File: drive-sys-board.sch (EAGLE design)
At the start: 27 parts

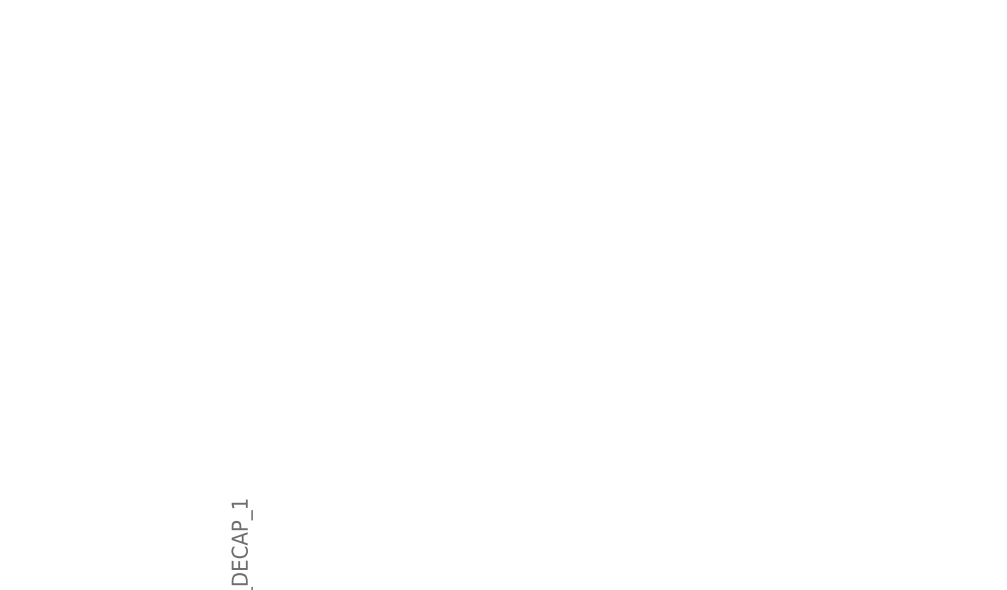
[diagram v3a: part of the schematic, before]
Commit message: okay nvm not finalized... almost used a IEA232 xcvr... need to use the added rs232 xcvr
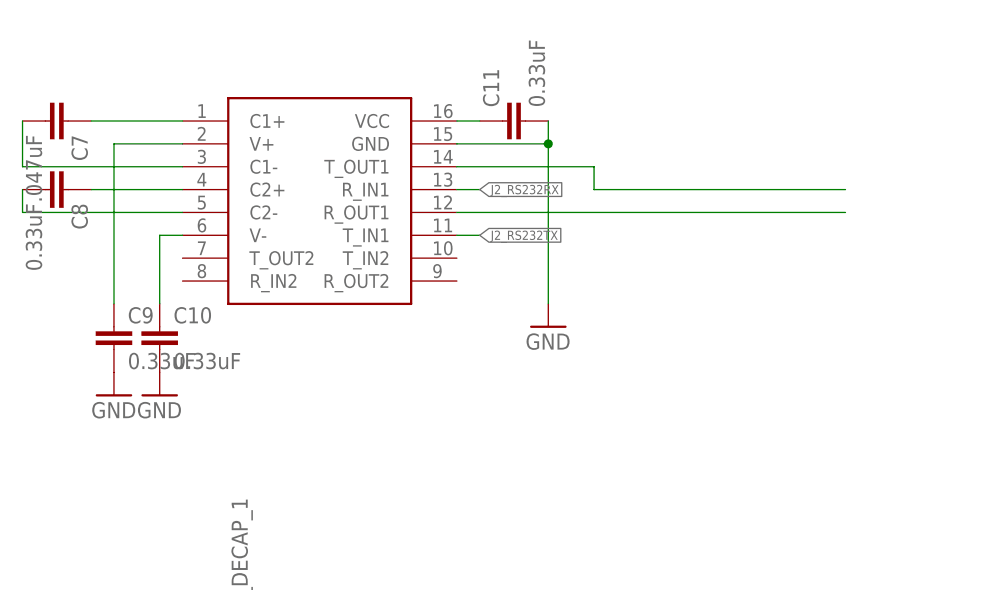
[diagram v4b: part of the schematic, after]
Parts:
- added C10, C11, C8, C9: 0.33uF, SparkFun-Capacitors:CAP1206
- added C7: .047uF, SparkFun-Capacitors:CAP1206
- added MAX232: MAX3232, MRDT-LIB2014:MAX3232
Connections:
- new net J2_RS232RX: MAX232.R_IN1
- new net J2_RS232TX: MAX232.T_IN1
- new net N$15: C7.2, MAX232.C1-
- new net N$16: C7.1, MAX232.C1+
- new net N$17: C8.1, MAX232.C2+
- new net N$18: C8.2, MAX232.C2-
- new net N$19: C10.1, MAX232.V-
- new net N$20: C9.1, MAX232.V+
- new net R_OUT1: MAX232.R_OUT1
- new net T_OUT1: MAX232.T_OUT1
- new net VCC1: C11.1, MAX232.VCC
- net GND: now also C10.2, C11.2, C9.2, MAX232.GND
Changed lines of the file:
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@@
 <part name="P+7" library="supply1" deviceset="+5V" device=""/>
 <part name="P+8" library="supply1" deviceset="+5V" device=""/>
+<part name="MAX232" library="MRDT-LIB2014" deviceset="MAX3232" device=""/>
+<part name="C7" library="SparkFun-Capacitors" deviceset="CAP" device="1206" value=".047uF"/>
+<part name="C8" library="SparkFun-Capacitors" deviceset="CAP" device="1206" value="0.33uF"/>
+<part name="C9" library="SparkFun-Capacitors" deviceset="CAP" device="1206" value="0.33uF"/>
+<part name="C10" library="SparkFun-Capacitors" deviceset="CAP" device="1206" value="0.33uF"/>
+<part name="C11" library="SparkFun-Capacitors" deviceset="CAP" device="1206" value="0.33uF"/>
+<part name="GND27" library="SparkFun-Aesthetics" deviceset="GND" device=""/>
+<part name="GND28" library="SparkFun-Aesthetics" deviceset="GND" device=""/>
+<part name="GND29" library="SparkFun-Aesthetics" deviceset="GND" device=""/>
 </parts>
 <sheets>
@@
 <instance part="P+7" gate="1" x="-73.66" y="43.18" rot="R90"/>
 <instance part="P+8" gate="1" x="-73.66" y="71.12" rot="R90"/>
+<instance part="MAX232" gate="G$1" x="-121.92" y="248.92"/>
+<instance part="C7" gate="G$1" x="-152.4" y="256.54" rot="R270"/>
+<instance part="C8" gate="G$1" x="-152.4" y="248.92" rot="R270"/>
+<instance part="C9" gate="G$1" x="-144.78" y="231.14"/>
+<instance part="C10" gate="G$1" x="-139.7" y="231.14"/>
+<instance part="C11" gate="G$1" x="-99.06" y="256.54" rot="R90"/>
+<instance part="GND27" gate="1" x="-144.78" y="226.06"/>
+<instance part="GND28" gate="1" x="-139.7" y="226.06"/>
+<instance part="GND29" gate="1" x="-96.52" y="233.68"/>
 </instances>
 <busses>
@@
 <pinref part="GND18" gate="1" pin="GND"/>
 </segment>
+<segment>
+<pinref part="C9" gate="G$1" pin="2"/>
+<pinref part="GND27" gate="1" pin="GND"/>
+</segment>
+<segment>
+<pinref part="C10" gate="G$1" pin="2"/>
+<pinref part="GND28" gate="1" pin="GND"/>
+</segment>
+<segment>
+<pinref part="MAX232" gate="G$1" pin="GND"/>
+<wire x1="-96.52" y1="254" x2="-106.68" y2="254" width="0.1524" layer="91"/>
+<pinref part="C11" gate="G$1" pin="2"/>
+<wire x1="-96.52" y1="254" x2="-96.52" y2="256.54" width="0.1524" layer="91"/>
+<wire x1="-96.52" y1="254" x2="-96.52" y2="236.22" width="0.1524" layer="91"/>
+<junction x="-96.52" y="254"/>
+<pinref part="GND29" gate="1" pin="GND"/>
+</segment>
 </net>
 <net name="TX_1" class="0">
@@
 </segment>
 </net>
+<net name="R_OUT1" class="0">
+<segment>
+<pinref part="MAX232" gate="G$1" pin="R_OUT1"/>
+<wire x1="-106.68" y1="246.38" x2="-63.5" y2="246.38" width="0.1524" layer="91"/>
+</segment>
+</net>
+<net name="N$15" class="0">
+<segment>
+<pinref part="MAX232" gate="G$1" pin="C1-"/>
+<pinref part="C7" gate="G$1" pin="2"/>
+<wire x1="-137.16" y1="251.46" x2="-154.94" y2="251.46" width="0.1524" layer="91"/>
+<wire x1="-154.94" y1="251.46" x2="-154.94" y2="256.54" width="0.1524" layer="91"/>
+</segment>
+</net>
+<net name="N$16" class="0">
+<segment>
+<pinref part="MAX232" gate="G$1" pin="C1+"/>
+<pinref part="C7" gate="G$1" pin="1"/>
+<wire x1="-137.16" y1="256.54" x2="-147.32" y2="256.54" width="0.1524" layer="91"/>
+</segment>
+</net>
+<net name="N$17" class="0">
+<segment>
+<pinref part="MAX232" gate="G$1" pin="C2+"/>
+<pinref part="C8" gate="G$1" pin="1"/>
+<wire x1="-137.16" y1="248.92" x2="-147.32" y2="248.92" width="0.1524" layer="91"/>
+</segment>
+</net>
+<net name="N$18" class="0">
+<segment>
+<pinref part="MAX232" gate="G$1" pin="C2-"/>
+<wire x1="-137.16" y1="246.38" x2="-154.94" y2="246.38" width="0.1524" layer="91"/>
+<pinref part="C8" gate="G$1" pin="2"/>
+<wire x1="-154.94" y1="246.38" x2="-154.94" y2="248.92" width="0.1524" layer="91"/>
+</segment>
+</net>
+<net name="N$19" class="0">
+<segment>
+<pinref part="MAX232" gate="G$1" pin="V-"/>
+<wire x1="-137.16" y1="243.84" x2="-139.7" y2="243.84" width="0.1524" layer="91"/>
+<wire x1="-139.7" y1="243.84" x2="-139.7" y2="236.22" width="0.1524" layer="91"/>
+<pinref part="C10" gate="G$1" pin="1"/>
+</segment>
+</net>
+<net name="N$20" class="0">
+<segment>
+<pinref part="MAX232" gate="G$1" pin="V+"/>
+<wire x1="-137.16" y1="254" x2="-144.78" y2="254" width="0.1524" layer="91"/>
+<wire x1="-144.78" y1="254" x2="-144.78" y2="236.22" width="0.1524" layer="91"/>
+<pinref part="C9" gate="G$1" pin="1"/>
+</segment>
+</net>
+<net name="VCC1" class="0">
+<segment>
+<pinref part="MAX232" gate="G$1" pin="VCC"/>
+<wire x1="-106.68" y1="256.54" x2="-104.14" y2="256.54" width="0.1524" layer="91"/>
+<pinref part="C11" gate="G$1" pin="1"/>
+</segment>
+</net>
+<net name="T_OUT1" class="0">
+<segment>
+<pinref part="MAX232" gate="G$1" pin="T_OUT1"/>
+<wire x1="-63.5" y1="248.92" x2="-91.44" y2="248.92" width="0.1524" layer="91"/>
+<wire x1="-106.68" y1="251.46" x2="-91.44" y2="251.46" width="0.1524" layer="91"/>
+<wire x1="-91.44" y1="251.46" x2="-91.44" y2="248.92" width="0.1524" layer="91"/>
+</segment>
+</net>
+<net name="J2_RS232TX" class="0">
+<segment>
+<pinref part="MAX232" gate="G$1" pin="T_IN1"/>
+<wire x1="-106.68" y1="243.84" x2="-104.14" y2="243.84" width="0.1524" layer="91"/>
+<label x="-104.14" y="243.84" size="1.016" layer="95" xref="yes"/>
+</segment>
+</net>
+<net name="J2_RS232RX" class="0">
+<segment>
+<pinref part="MAX232" gate="G$1" pin="R_IN1"/>
+<wire x1="-106.68" y1="248.92" x2="-104.14" y2="248.92" width="0.1524" layer="91"/>
+<label x="-104.14" y="248.92" size="1.016" layer="95" xref="yes"/>
+</segment>
+</net>

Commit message: final rs232 version
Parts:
- removed C10, C11, C8, C9: 0.33uF, SparkFun-Capacitors:CAP1206
- removed C7: .047uF, SparkFun-Capacitors:CAP1206
- removed MAX232: MAX3232, MRDT-LIB2014:MAX3232
- MAX232_1, MAX232_2, MAX232_3: value MAX232SOIC16 -> MAX3232SO16; device SparkFun-DigitalIC:MAX232SOIC16 -> MRDT-Digital-ICs:MAX3232SO16
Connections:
- removed net J2_RS232RX: MAX232.R_IN1
- removed net J2_RS232TX: MAX232.T_IN1
- removed net N$15: C7.2, MAX232.C1-
- removed net N$16: C7.1, MAX232.C1+
- removed net N$17: C8.1, MAX232.C2+
- removed net N$18: C8.2, MAX232.C2-
- removed net N$19: C10.1, MAX232.V-
- removed net N$20: C9.1, MAX232.V+
- removed net R_OUT1: MAX232.R_OUT1
- removed net T_OUT1: MAX232.T_OUT1
- removed net VCC1: C11.1, MAX232.VCC
- net GND: no longer C10.2, C11.2, C9.2, MAX232.GND, MAX232_2.GND, MAX232_3.GND
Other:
- moved on the sheet: MAX232_C1_1, MAX232_C1_2, MAX232_C1_3, MAX232_C2_1, MAX232_C2_2, MAX232_C2_3, MAX232_DECAP_1, MAX232_DECAP_2, MAX232_DECAP_3, MAX232_VNCAP_1, MAX232_VNCAP_2, MAX232_VNCAP_3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

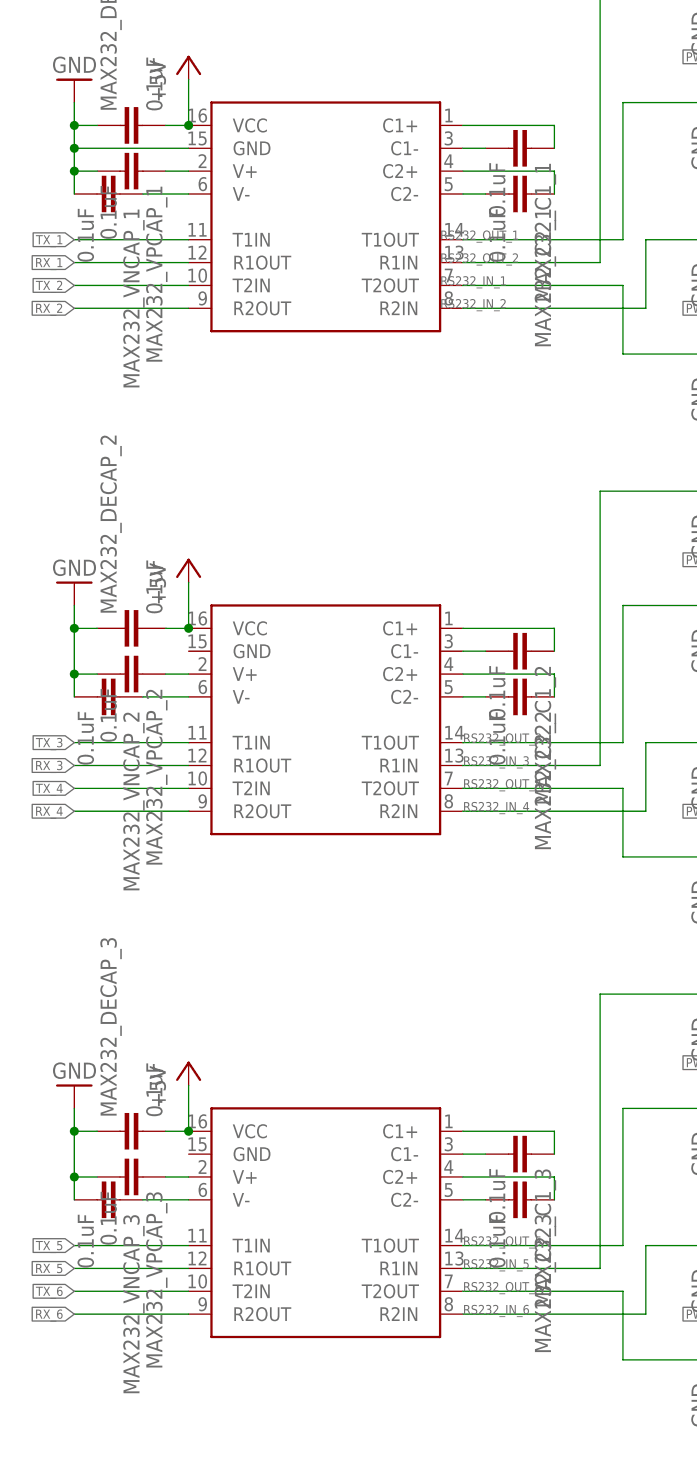
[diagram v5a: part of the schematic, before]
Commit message: finished swapping for max3232's, final rev2
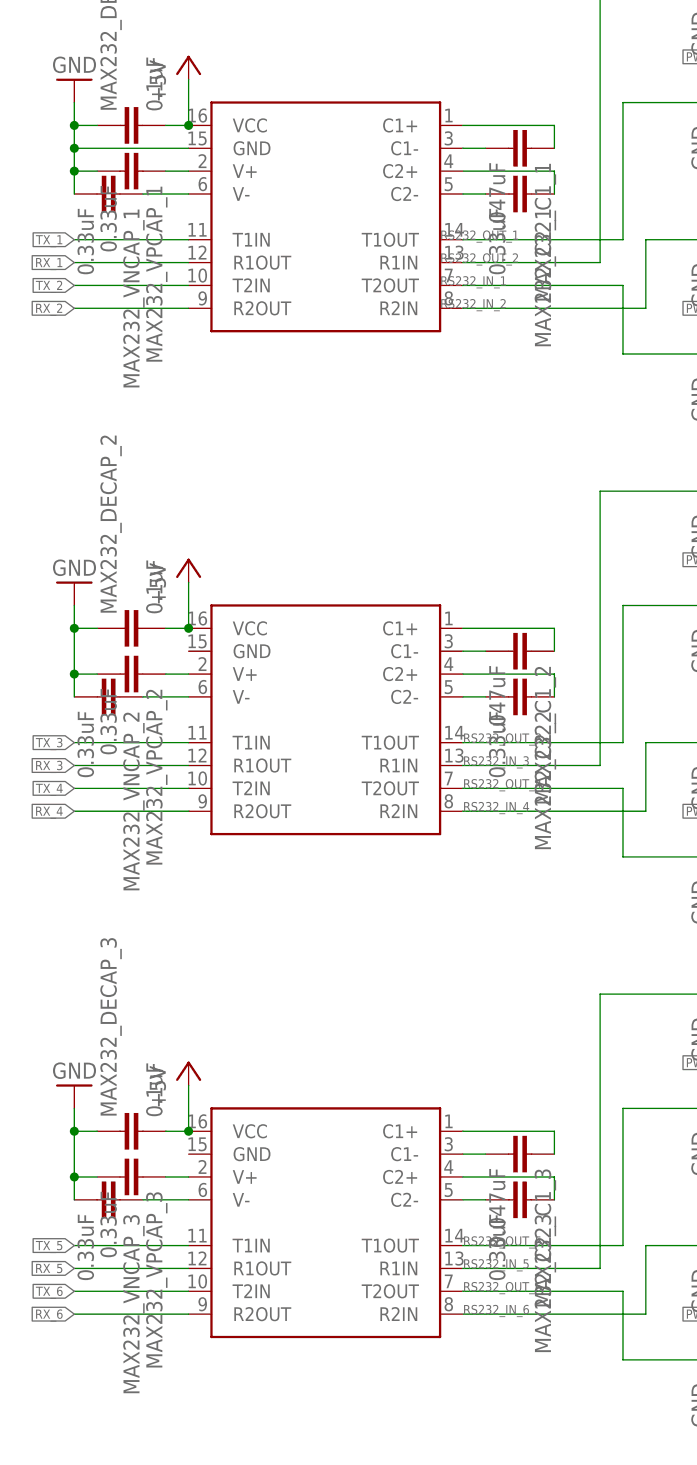
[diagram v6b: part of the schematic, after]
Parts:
- MAX232_C1_1, MAX232_C1_2: value 0.1uF -> .047uF
- MAX232_C1_3: value 0.1uF -> 0.047uF
- MAX232_C2_1, MAX232_C2_2, MAX232_C2_3, MAX232_VNCAP_1, MAX232_VNCAP_2, MAX232_VNCAP_3, MAX232_VPCAP_1, MAX232_VPCAP_2, MAX232_VPCAP_3: value 0.1uF -> 0.33uF
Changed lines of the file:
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@@
 <part name="H1" library="holes" deviceset="MOUNT-HOLE" device="3.2"/>
 <part name="MAX232_1" library="MRDT-Digital-ICs" deviceset="MAX3232" device="SO16"/>
-<part name="MAX232_C1_1" library="SparkFun-Capacitors" deviceset="CAP" device="1206" value="0.1uF"/>
-<part name="MAX232_C2_1" library="SparkFun-Capacitors" deviceset="CAP" device="1206" value="0.1uF"/>
-<part name="MAX232_VNCAP_1" library="SparkFun-Capacitors" deviceset="CAP" device="1206" value="0.1uF"/>
-<part name="MAX232_VPCAP_1" library="SparkFun-Capacitors" deviceset="CAP" device="1206" value="0.1uF"/>
+<part name="MAX232_C1_1" library="SparkFun-Capacitors" deviceset="CAP" device="1206" value=".047uF"/>
+<part name="MAX232_C2_1" library="SparkFun-Capacitors" deviceset="CAP" device="1206" value="0.33uF"/>
+<part name="MAX232_VNCAP_1" library="SparkFun-Capacitors" deviceset="CAP" device="1206" value="0.33uF"/>
+<part name="MAX232_VPCAP_1" library="SparkFun-Capacitors" deviceset="CAP" device="1206" value="0.33uF"/>
 <part name="MAX232_DECAP_1" library="SparkFun-Capacitors" deviceset="CAP" device="1206" value="0.1uF"/>
 <part name="P+15" library="supply1" deviceset="+5V" device=""/>
@@
 <part name="U$1" library="MRDT-2015-General" deviceset="TIVA-C-CONNECTED" device=""/>
 <part name="MAX232_2" library="MRDT-Digital-ICs" deviceset="MAX3232" device="SO16"/>
-<part name="MAX232_C1_2" library="SparkFun-Capacitors" deviceset="CAP" device="1206" value="0.1uF"/>
-<part name="MAX232_C2_2" library="SparkFun-Capacitors" deviceset="CAP" device="1206" value="0.1uF"/>
-<part name="MAX232_VNCAP_2" library="SparkFun-Capacitors" deviceset="CAP" device="1206" value="0.1uF"/>
-<part name="MAX232_VPCAP_2" library="SparkFun-Capacitors" deviceset="CAP" device="1206" value="0.1uF"/>
+<part name="MAX232_C1_2" library="SparkFun-Capacitors" deviceset="CAP" device="1206" value=".047uF"/>
+<part name="MAX232_C2_2" library="SparkFun-Capacitors" deviceset="CAP" device="1206" value="0.33uF"/>
+<part name="MAX232_VNCAP_2" library="SparkFun-Capacitors" deviceset="CAP" device="1206" value="0.33uF"/>
+<part name="MAX232_VPCAP_2" library="SparkFun-Capacitors" deviceset="CAP" device="1206" value="0.33uF"/>
 <part name="MAX232_DECAP_2" library="SparkFun-Capacitors" deviceset="CAP" device="1206" value="0.1uF"/>
 <part name="GND2" library="supply1" deviceset="GND" device=""/>
@@
 <part name="P+5" library="supply1" deviceset="+5V" device=""/>
 <part name="MAX232_3" library="MRDT-Digital-ICs" deviceset="MAX3232" device="SO16"/>
-<part name="MAX232_C1_3" library="SparkFun-Capacitors" deviceset="CAP" device="1206" value="0.1uF"/>
-<part name="MAX232_C2_3" library="SparkFun-Capacitors" deviceset="CAP" device="1206" value="0.1uF"/>
-<part name="MAX232_VNCAP_3" library="SparkFun-Capacitors" deviceset="CAP" device="1206" value="0.1uF"/>
-<part name="MAX232_VPCAP_3" library="SparkFun-Capacitors" deviceset="CAP" device="1206" value="0.1uF"/>
+<part name="MAX232_C1_3" library="SparkFun-Capacitors" deviceset="CAP" device="1206" value="0.047uF"/>
+<part name="MAX232_C2_3" library="SparkFun-Capacitors" deviceset="CAP" device="1206" value="0.33uF"/>
+<part name="MAX232_VNCAP_3" library="SparkFun-Capacitors" deviceset="CAP" device="1206" value="0.33uF"/>
+<part name="MAX232_VPCAP_3" library="SparkFun-Capacitors" deviceset="CAP" device="1206" value="0.33uF"/>
 <part name="MAX232_DECAP_3" library="SparkFun-Capacitors" deviceset="CAP" device="1206" value="0.1uF"/>
 <part name="GND14" library="supply1" deviceset="GND" device=""/>
